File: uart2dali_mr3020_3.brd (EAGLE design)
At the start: 52 x 70 mm, 81 parts, among them IC2 LM393D, IC3 SFH6156, IC4 SFH6156, J1 AVR_SPI_PRG_6NS, Q1 SST201, Q2 BSP170P, Q3 BC817-25SMD, X2 22-23-2021

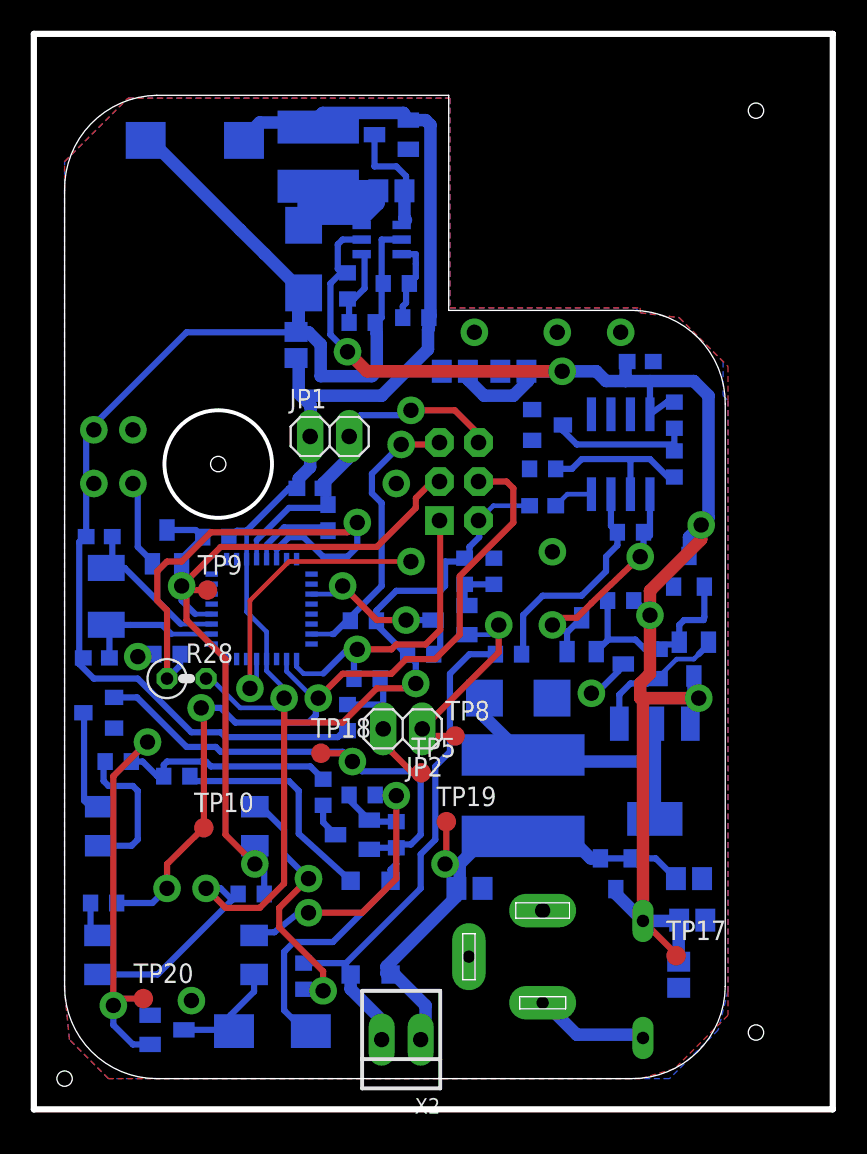
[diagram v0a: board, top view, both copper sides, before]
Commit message: - added some comments - fixes on layout
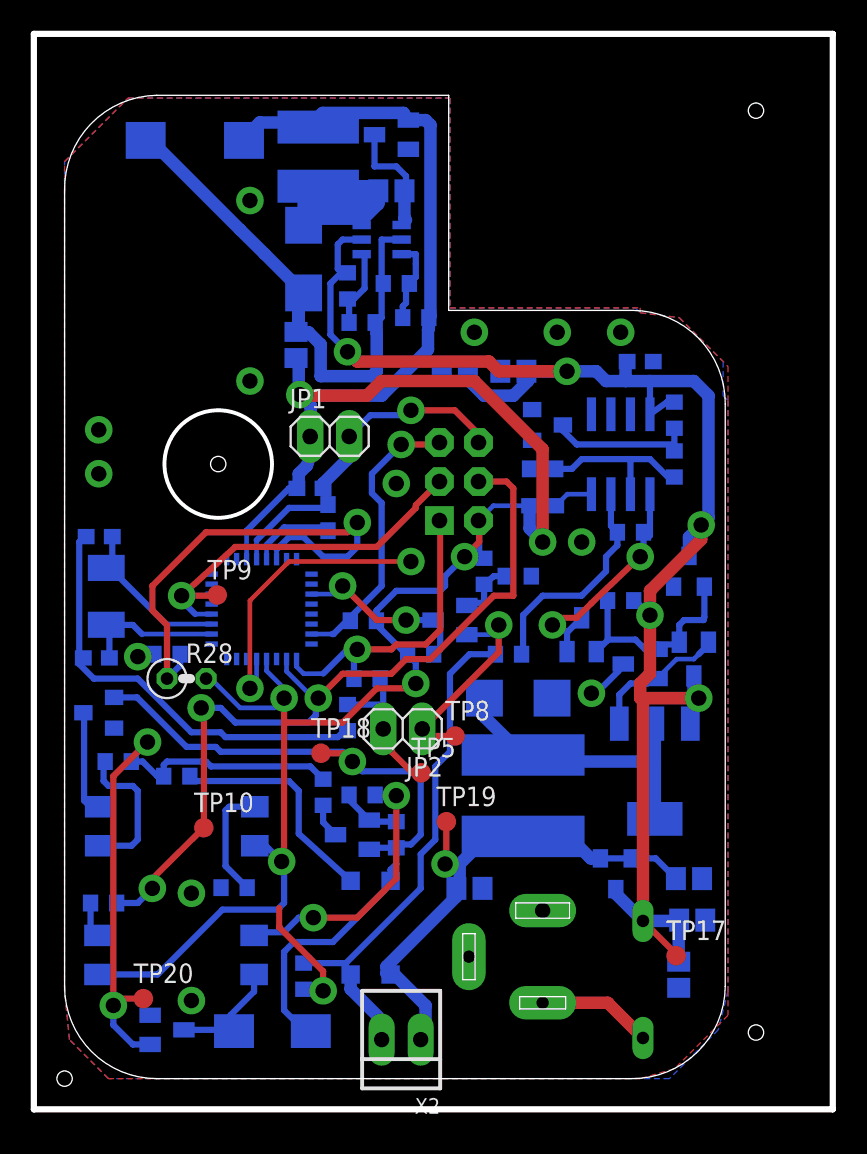
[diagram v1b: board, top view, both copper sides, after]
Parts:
- removed R27: 10k, resistor:R0603
- removed T4: (no value), transistor:SOT23-BEC
- moved R8 1.62 mm to (29.5, 32.7), turned to 180 degrees
- moved R9 1.27 mm to (27.3, 33.0)
- moved R26 1.19 mm to (11.0, 12.4), turned to 0 degrees
- moved TP9 0.71 mm to (9.94, 31.5)
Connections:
- new net N$7: IC4.3, R26.1
- net +5V: now also IC4.4; no longer R26.1, R27.1
- net DALI_RCV: no longer IC4.4, R26.2, R27.2, T4.B, T4.C
- net GND: now also R26.2; no longer IC4.3, T4.E
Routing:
- net GND: track 159.9 -> 121.6 mm
- net DALI_RCV: track 55.3 -> 24.8 mm, vias 2 -> 1
- net +5V: track 135.5 -> 153.6 mm, vias 3 -> 7
- net N$7: track 0.00 -> 7.62 mm
- net N$20: track 3.34 -> 4.27 mm

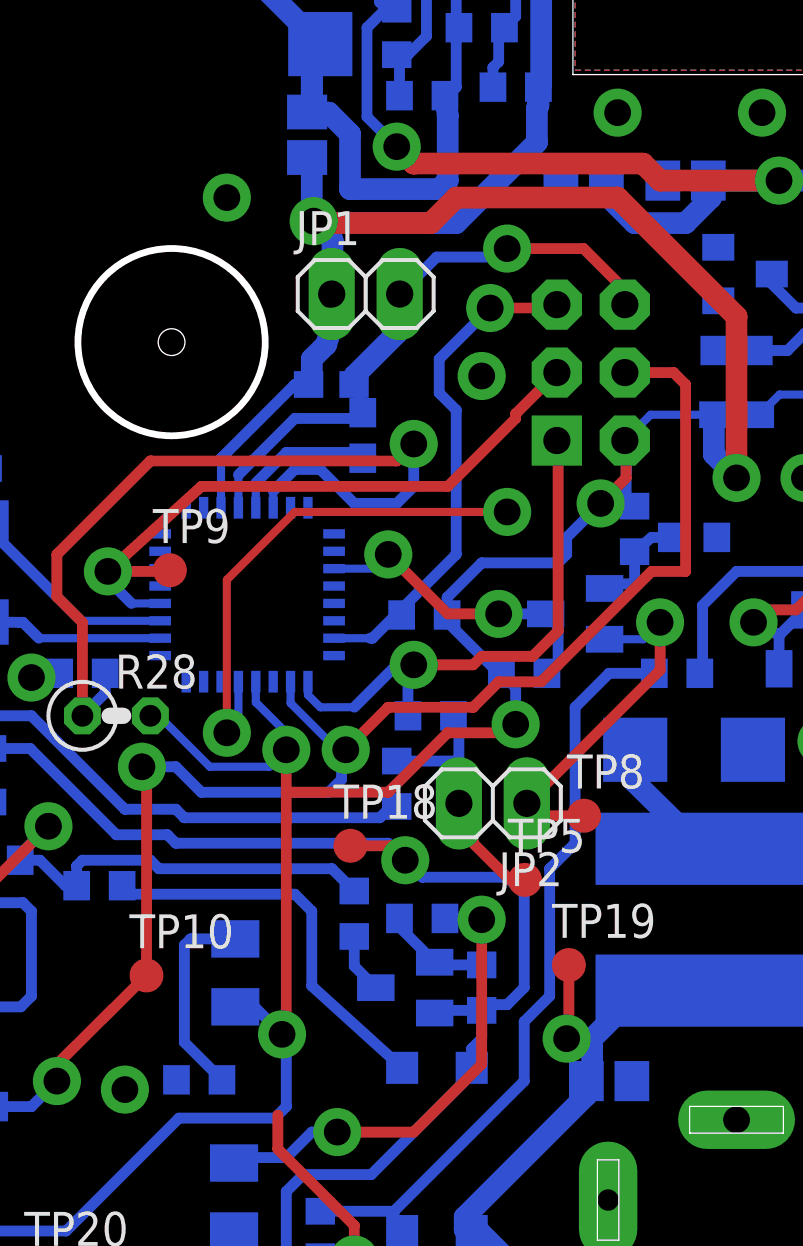
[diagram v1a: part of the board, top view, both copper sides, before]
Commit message: - updated schematics and layout - some bugfixes in firmware
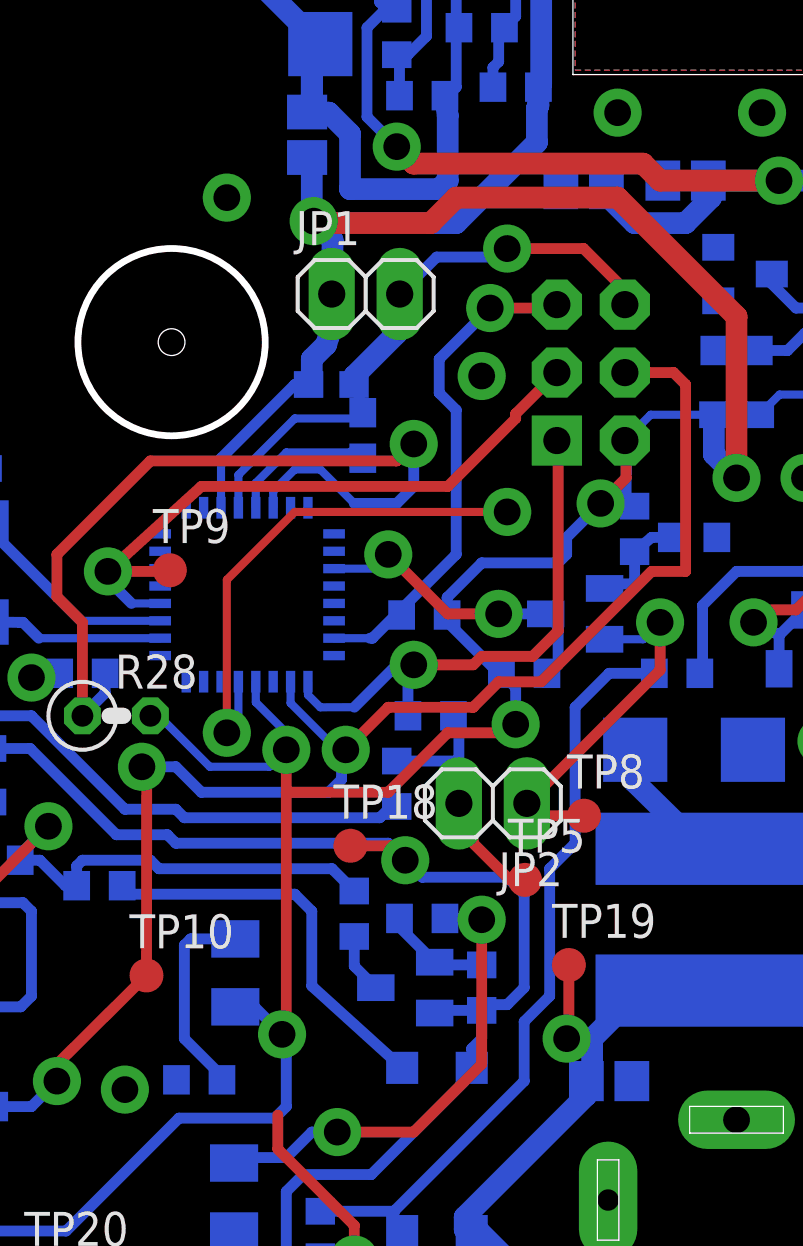
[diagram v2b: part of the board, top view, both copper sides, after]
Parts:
- T1, T2: value (none) -> MMBT3904LT1
- T3: value (none) -> MMBT3640LT1
- moved C14 0.32 mm to (25.4, 45.7)
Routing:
- net +5V: vias 7 -> 6
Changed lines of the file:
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@@
 <?xml version="1.0" encoding="utf-8"?>
 <!DOCTYPE eagle SYSTEM "eagle.dtd">
-<eagle version="6.3">
+<eagle version="6.4">
 <drawing>
 <settings>
@@
 <element name="R10" library="resistor" package="R0603" value="10k" x="23.1775" y="27.6225" rot="MR0"/>
 <element name="R8" library="resistor" package="R0603" value="2k2" x="29.5275" y="32.7025" rot="MR180"/>
-<element name="T1" library="transistor" package="SOT23-BEC" value="" x="25.0825" y="29.845" rot="MR270"/>
+<element name="T1" library="transistor" package="SOT23-BEC" value="MMBT3904LT1" x="25.0825" y="29.845" rot="MR270"/>
 <element name="IC2" library="linear" package="SO08" value="LM393D" x="36.195" y="40.64" rot="MR0"/>
-<element name="T3" library="transistor" package="SOT23-BEC" value="" x="37.465" y="26.9875" rot="MR270"/>
-<element name="T2" library="transistor" package="SOT23-BEC" value="" x="40.9575" y="27.305" rot="MR180"/>
+<element name="T3" library="transistor" package="SOT23-BEC" value="MMBT3640LT1" x="37.465" y="26.9875" rot="MR270"/>
+<element name="T2" library="transistor" package="SOT23-BEC" value="MMBT3904LT1" x="40.9575" y="27.305" rot="MR180"/>
 <element name="Q2" library="transistor-fet" package="SOT223" value="BSP170P" x="38.4175" y="20.0025" rot="MR180"/>
 <element name="Q1" library="transistor-fet" package="SOT23" value="SST201" x="33.655" y="28.8925" rot="MR0"/>
@@
 <element name="D8" library="diode" package="TO236" value="BZX84CSMD" x="35.8775" y="13.335" rot="MR180"/>
 <element name="C13" library="resistor" package="C0805" value="" x="26.3525" y="12.3825" rot="MR0"/>
-<element name="C14" library="resistor" package="C0805" value="" x="25.4" y="46.0375" rot="MR0"/>
+<element name="C14" library="resistor" package="C0805" value="" x="25.4" y="45.72" rot="MR0"/>
 <element name="C15" library="resistor" package="C0805" value="" x="29.21" y="46.0375" rot="MR0"/>
 <element name="X2" library="con-molex" package="22-23-2021" value="22-23-2021" x="21.9075" y="2.54" rot="R180">
@@
 <wire x1="16.93" y1="38.3075" x2="16.82" y2="38.4175" width="0.4064" layer="16"/>
 <wire x1="12.4975" y1="33.81" x2="12.4975" y2="35.04" width="0.3048" layer="16"/>
-<wire x1="12.4975" y1="35.04" x2="14.605" y2="37.1475" width="0.4064" layer="16"/>
-<wire x1="14.605" y1="37.1475" x2="16.93" y2="37.1475" width="0.4064" layer="16"/>
+<wire x1="12.4975" y1="35.04" x2="14.605" y2="37.1475" width="0.3048" layer="16"/>
+<wire x1="14.605" y1="37.1475" x2="16.93" y2="37.1475" width="0.3048" layer="16"/>
 <wire x1="16.93" y1="37.1475" x2="17.145" y2="37.3625" width="0.4064" layer="16"/>
 <wire x1="12.4975" y1="27.31" x2="12.4975" y2="25.8325" width="0.3048" layer="16"/>
@@
 <wire x1="30.2675" y1="37.2875" x2="30.2675" y2="35.8075" width="0.8128" layer="16"/>
 <wire x1="30.2675" y1="35.8075" x2="30.7975" y2="35.2775" width="0.8128" layer="16"/>
-<wire x1="15.875" y1="41.5925" x2="15.875" y2="41.6875" width="0.8128" layer="16"/>
 <wire x1="15.875" y1="41.6875" x2="15.985" y2="41.7975" width="0.8128" layer="16"/>
-<via x="15.875" y="41.5925" extent="1-16" drill="0.6" shape="square"/>
 <contactref element="IC4" pad="4"/>
 <wire x1="12.3825" y1="15.1575" x2="13.1" y2="15.1575" width="0.4064" layer="16"/>
@@
 <wire x1="26.94" y1="36.2425" x2="26.9875" y2="36.195" width="0.4064" layer="1"/>
 <wire x1="26.9875" y1="36.195" x2="26.9875" y2="34.925" width="0.4064" layer="1"/>
-<wire x1="15.875" y1="41.5925" x2="15.875" y2="40.225" width="0.8128" layer="16"/>
+<wire x1="15.875" y1="41.6875" x2="15.875" y2="40.225" width="0.8128" layer="16"/>
 <wire x1="15.875" y1="40.225" x2="15.7775" y2="39.9075" width="0.8128" layer="16"/>
 <wire x1="15.7775" y1="39.9075" x2="15.24" y2="39.37" width="0.8128" layer="16"/>
@@
 <wire x1="17.30375" y1="48.41875" x2="17.30375" y2="51.7525" width="0.4064" layer="16"/>
 <wire x1="17.30375" y1="51.7525" x2="18.018125" y2="52.466875" width="0.4064" layer="16"/>
-<wire x1="26.25" y1="46.0375" x2="26.25" y2="45.505" width="0.8128" layer="16"/>
+<wire x1="26.25" y1="45.72" x2="26.25" y2="45.505" width="0.8128" layer="16"/>
 <wire x1="26.25" y1="45.505" x2="27.305" y2="44.45" width="0.8128" layer="16"/>
 <wire x1="27.305" y1="44.45" x2="29.21" y2="44.45" width="0.8128" layer="16"/>
@@
 <wire x1="19.05" y1="34.6075" x2="18.415" y2="33.9725" width="0.4064" layer="16"/>
 <wire x1="18.415" y1="33.9725" x2="16.8275" y2="33.9725" width="0.4064" layer="16"/>
-<wire x1="16.8275" y1="33.9725" x2="15.5575" y2="35.2425" width="0.4064" layer="16"/>
-<wire x1="15.5575" y1="35.2425" x2="14.605" y2="35.2425" width="0.4064" layer="16"/>
-<wire x1="14.605" y1="35.2425" x2="13.7975" y2="34.435" width="0.4064" layer="16"/>
+<wire x1="16.8275" y1="33.9725" x2="15.5575" y2="35.2425" width="0.3048" layer="16"/>
+<wire x1="15.5575" y1="35.2425" x2="14.605" y2="35.2425" width="0.3048" layer="16"/>
+<wire x1="14.605" y1="35.2425" x2="13.7975" y2="34.435" width="0.3048" layer="16"/>
 <wire x1="13.7975" y1="33.81" x2="13.7975" y2="34.435" width="0.3048" layer="16"/>
 <wire x1="6.6675" y1="29.5275" x2="6.6675" y2="26.035" width="0.4064" layer="1"/>
@@
 <contactref element="C16" pad="2"/>
 <wire x1="13.1475" y1="33.81" x2="13.1475" y2="34.7375" width="0.3048" layer="16"/>
-<wire x1="13.1475" y1="34.7375" x2="14.2875" y2="35.8775" width="0.4064" layer="16"/>
-<wire x1="14.2875" y1="35.8775" x2="16.725" y2="35.8775" width="0.4064" layer="16"/>
+<wire x1="13.1475" y1="34.7375" x2="14.2875" y2="35.8775" width="0.3048" layer="16"/>
+<wire x1="14.2875" y1="35.8775" x2="16.725" y2="35.8775" width="0.3048" layer="16"/>
 <wire x1="16.725" y1="35.8775" x2="17.145" y2="35.6625" width="0.4064" layer="16"/>
 </signal>
@@
 <wire x1="12.3825" y1="17.6975" x2="10.7125" y2="17.6975" width="0.4064" layer="16"/>
 <wire x1="10.7125" y1="17.6975" x2="10.4775" y2="17.4625" width="0.4064" layer="16"/>
-<wire x1="10.4775" y1="17.4625" x2="10.4775" y2="13.835" width="0.4064" layer="16"/>
-<wire x1="10.4775" y1="13.835" x2="11.8825" y2="12.43" width="0.4064" layer="16"/>
+<wire x1="10.4775" y1="17.4625" x2="10.4775" y2="13.97" width="0.4064" layer="16"/>
+<wire x1="10.4775" y1="13.97" x2="11.8825" y2="12.565" width="0.4064" layer="16"/>
+<wire x1="11.8825" y1="12.565" x2="11.8825" y2="12.43" width="0.4064" layer="16"/>
 </signal>
 </signals>
